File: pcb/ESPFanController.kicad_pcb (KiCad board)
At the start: 2 copper layers, 22.5 x 42 mm, 25 parts, among them J1 Serial, J2 12Vin, M1 Fan1, M2 Fan2, M3 Fan3, SW1 SW_Push, U1 AMS1117-3.3, U2 ESP32-WROOM-32

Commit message: feat: add position for pullups
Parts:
- added R7: 4k7, Resistor_SMD:R_0402_1005Metric_Pad0.72x0.64mm_HandSolder, F.Cu at (166.8, 98.0)
- added R8: 4k7, Resistor_SMD:R_0402_1005Metric_Pad0.72x0.64mm_HandSolder, F.Cu at (166.8, 97.0)
- SW1: value SW_Push -> Boot
- moved G*** 0.35 mm to (170.5, 96.2)
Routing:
- net /RX: track 51.6 -> 53.9 mm
- net /TX: track 51.9 -> 53.8 mm
- net +3V3: track 18.3 -> 20.1 mm, vias 7 -> 9

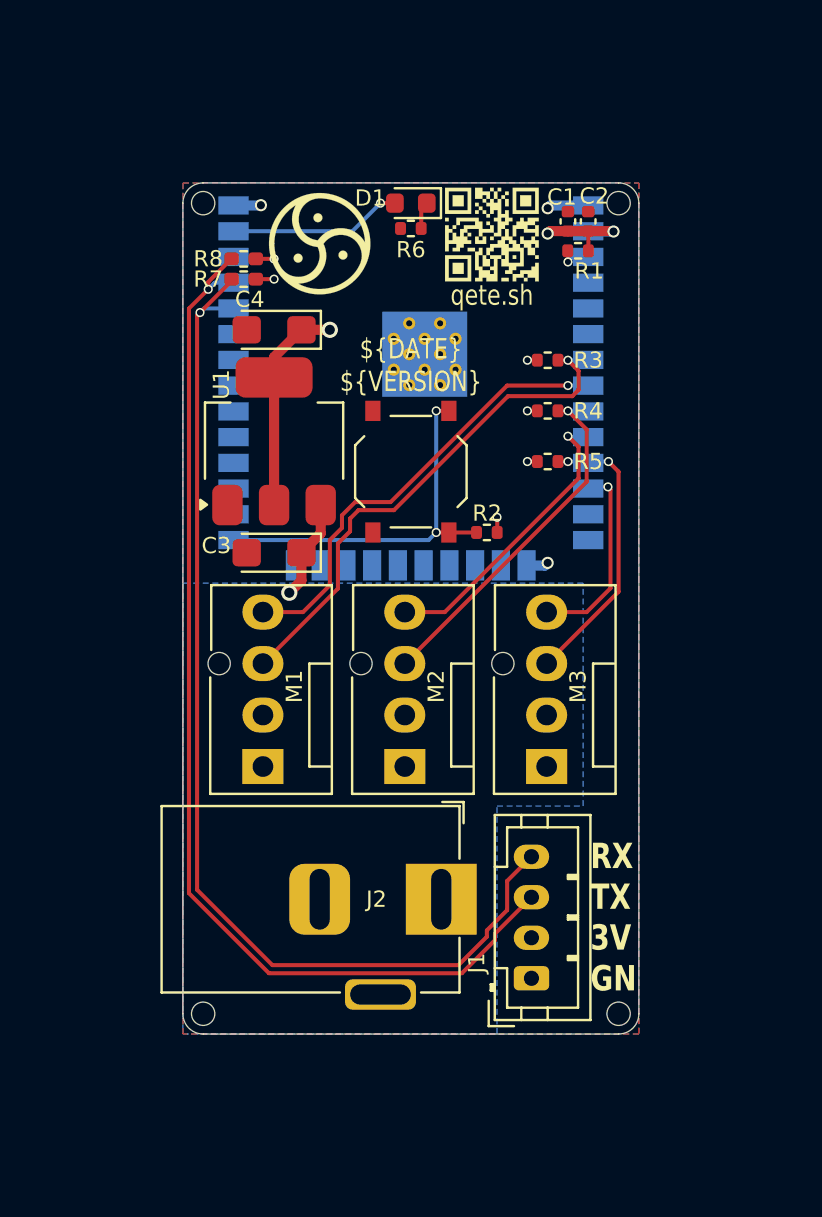
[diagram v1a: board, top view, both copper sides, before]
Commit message: feat: add edge rails
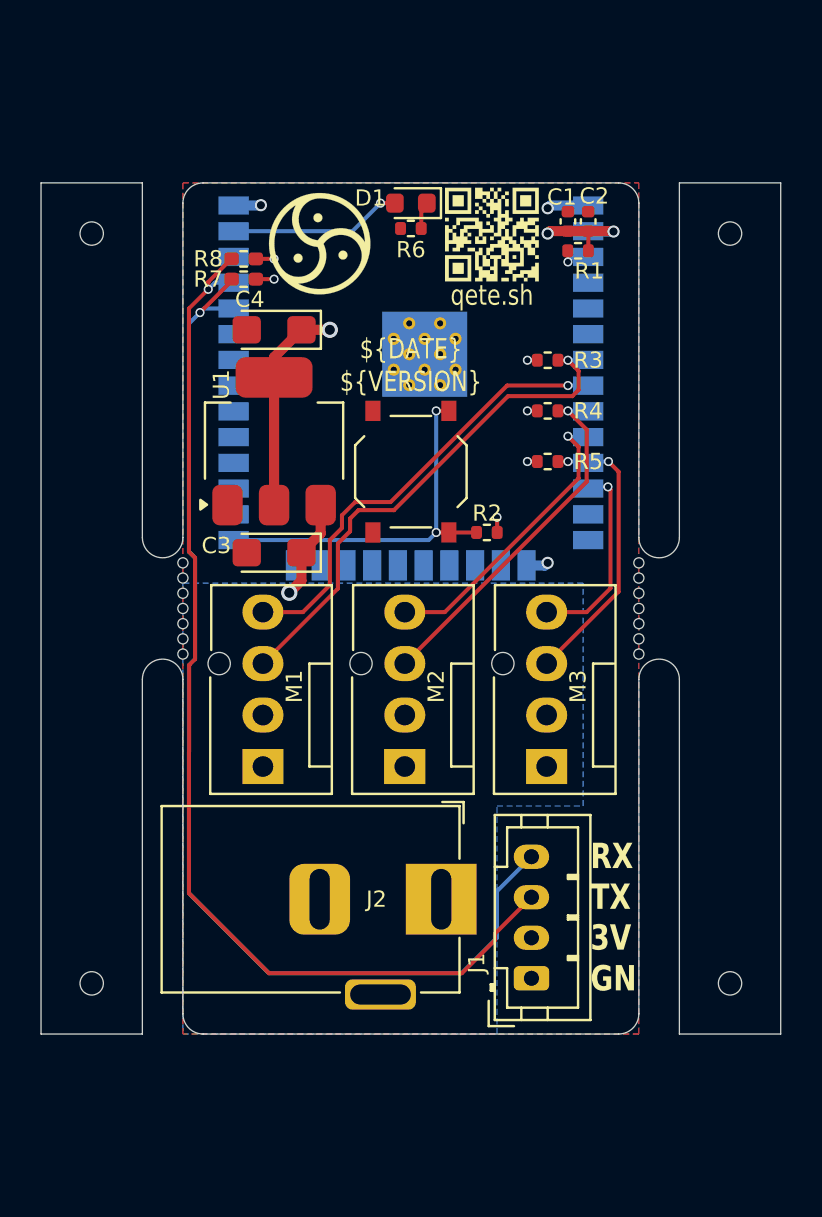
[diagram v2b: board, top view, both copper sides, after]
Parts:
- removed the REF** at (164.8, 134.2)
- removed the REF** at (185.2, 134.2)
- removed the REF** at (164.8, 94.2)
- removed the REF** at (185.2, 94.2)
- added REF**: JLCPCB_Tooling_Hole, My_Footprints:JLCPCB_Tooling_Hole, F.Cu at (159.2, 95.8)
- added REF**: JLCPCB_Tooling_Hole, My_Footprints:JLCPCB_Tooling_Hole, F.Cu at (159.2, 132.8)
- added REF**: JLCPCB_Tooling_Hole, My_Footprints:JLCPCB_Tooling_Hole, F.Cu at (190.8, 132.8)
- added REF**: JLCPCB_Tooling_Hole, My_Footprints:JLCPCB_Tooling_Hole, F.Cu at (190.8, 95.8)
- added mouse-bite-2mm-slot: VAL**, Panelization:mouse-bite-2x5mm-slot-onesided-v2, F.Cu at (162.8, 114.2)
- added mouse-bite-2mm-slot: VAL**, Panelization:mouse-bite-2x5mm-slot-onesided-v2, F.Cu at (187.2, 114.2)
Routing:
- net /RX: track 53.9 -> 55.4 mm
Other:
- board size 22.5 x 42 mm -> 36.5 x 42 mm

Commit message: feat: add second LED
feat: add cutouts to the corners

feat: add optional pull-ups to serial pins
  for I2C use after programming
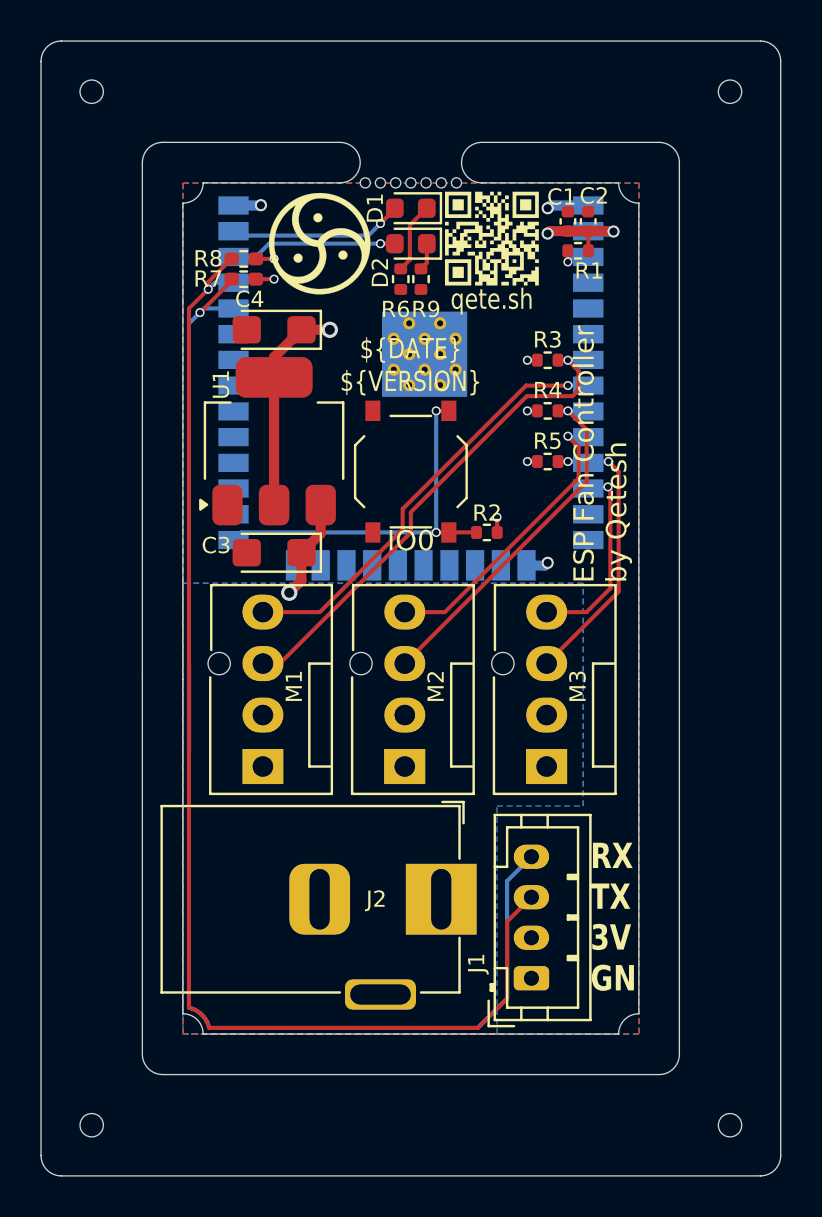
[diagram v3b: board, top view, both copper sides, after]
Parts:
- removed the mouse-bite-2mm-slot at (187.2, 114.2)
- added D2: Yellow, LED_SMD:LED_0603_1608Metric, F.Cu at (175.0, 96.2)
- added R9: 680R, Resistor_SMD:R_0402_1005Metric, F.Cu at (175.5, 98.0)
- D1: value LED_Small -> Red
- moved mouse-bite-2mm-slot 25.2 mm to (175.0, 92.2), turned to 180 degrees
- moved REF** 7.00 mm to (159.2, 88.8)
- moved REF** 7.00 mm to (159.2, 139.8)
- moved REF** 7.00 mm to (190.8, 139.8)
- moved REF** 7.00 mm to (190.8, 88.8)
- moved R6 2.55 mm to (174.5, 98.0), turned to -90 degrees
- moved D1 0.25 mm to (175.0, 94.5)
- moved G*** 0.20 mm to (179.0, 96.0)
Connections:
- net /LED renamed /Red
- U2 pad 36: unconnected-(U2-IO22-Pad36) -> /Yellow
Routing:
- net /Yellow: track 0.00 -> 8.23 mm, vias 0 -> 1
- net /RX: track 55.4 -> 61.4 mm
- net /TX: track 54.1 -> 60.0 mm
- net Net-(D1-K): track 1.02 -> 3.52 mm
- net Net-(D2-K): track 0.00 -> 1.36 mm
- net /PWM1: track 22.4 -> 21.3 mm
- net /Tacho1: track 26.1 -> 25.0 mm
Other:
- board size 36.5 x 42 mm -> 36.5 x 56 mm
- board text added: "ESP Fan Controller by Qetesh"
- board text added: "IO0"
